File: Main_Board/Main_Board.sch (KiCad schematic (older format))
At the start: 68 parts, among them IC1 AZ1085CD-3.3TRG1, J1 PJ-037A, U1 STM32L152ZCTx, U2 LM386, Y1 ABM10W-16.0000MHZ-4-B1U-T3

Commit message: Reset_Line
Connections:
- net GND: no longer GPIOHeader1.1 (Pin_1)
- net Reset_Line: now reaches U1.87 (PG2)
- net Reset_Line: now also GPIOHeader1.1 (Pin_1)
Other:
- note added: "Speaker Circuit"
- note removed: "Hall Out Values"
- moved on the sheet: 5VOut1, BL1, BR1, C11, C24, C25, GPIOHeader1, J1, R8, TL1, TR1, Y1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

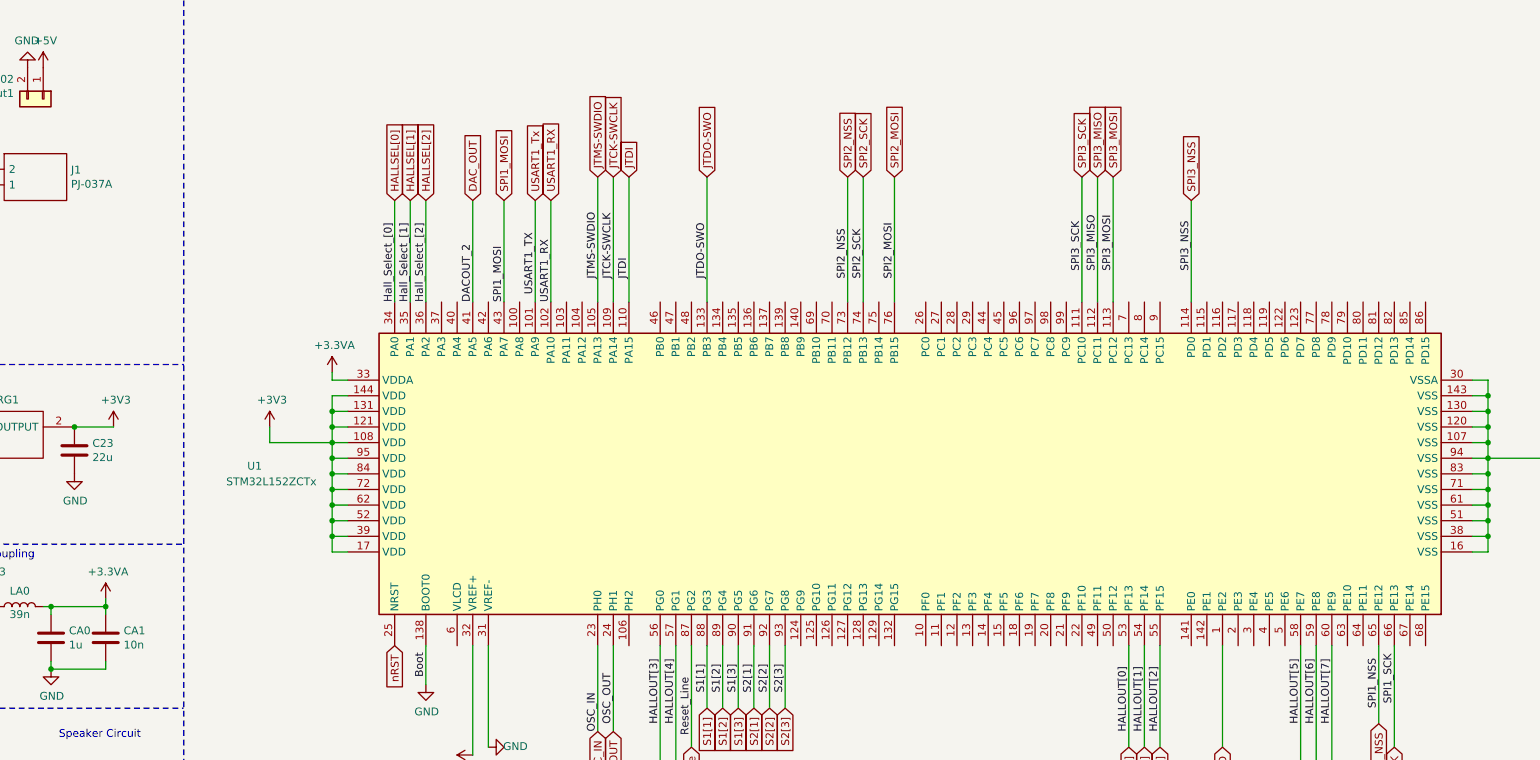
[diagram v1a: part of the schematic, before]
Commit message: final Rev1 changes. increased heatsink area, flipped LEDs again, increased button mount hole size
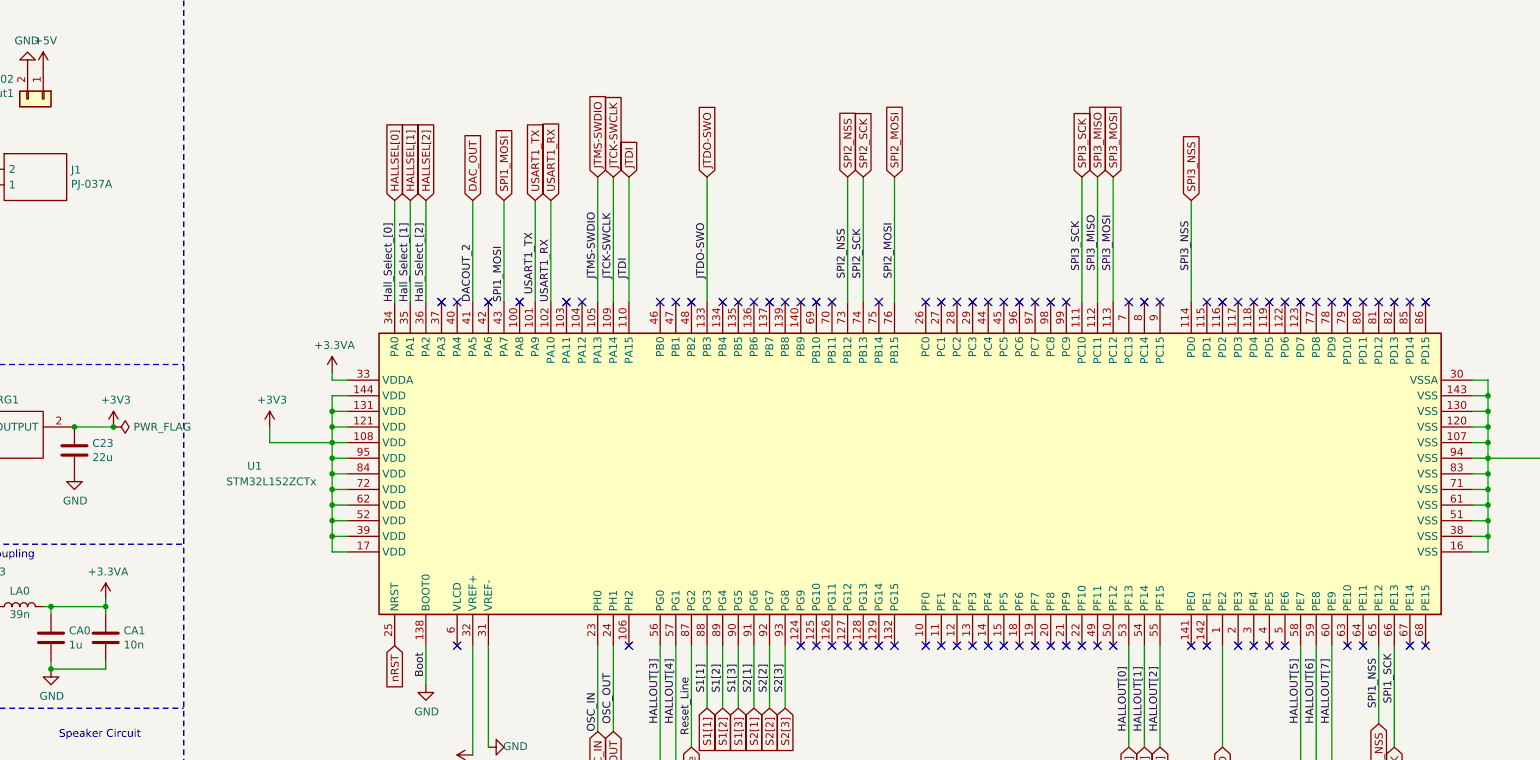
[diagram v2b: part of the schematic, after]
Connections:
- no-connect marks 3 -> 81
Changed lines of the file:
@@
 Analog Decoupling
 Text GLabel 15800 3900 1    50   Input ~ 0
-USART1_Tx
+USART1_TX
 Text GLabel 15900 3900 1    50   Input ~ 0
 USART1_RX
@@
 	1    0    0    -1
 $EndComp
-Wire Wire Line
-	12850 5350 13100 5350
 Connection ~ 12850 5350
 $Comp
@@
 Text GLabel 1400 8800 3    50   Input ~ 0
 Reset_Line
+$Comp
+L power:PWR_FLAG #FLG0101
+U 1 1 616BB65E
+P 13100 5350
+F 0 "#FLG0101" H 13100 5425 50  0001 C CNN
+F 1 "PWR_FLAG" V 13100 5478 50  0000 L CNN
+F 2 "" H 13100 5350 50  0001 C CNN
+F 3 "~" H 13100 5350 50  0001 C CNN
+	1    13100 5350
+	0    1    1    0
+$EndComp
+Connection ~ 13100 5350
+Wire Wire Line
+	12850 5350 13100 5350
+NoConn ~ 15200 4550
+NoConn ~ 15300 4550
+NoConn ~ 15500 4550
+NoConn ~ 15700 4550
+NoConn ~ 16000 4550
+NoConn ~ 16100 4550
+NoConn ~ 16600 4550
+NoConn ~ 16700 4550
+NoConn ~ 16800 4550
+NoConn ~ 17000 4550
+NoConn ~ 17100 4550
+NoConn ~ 17200 4550
+NoConn ~ 17300 4550
+NoConn ~ 17400 4550
+NoConn ~ 17500 4550
+NoConn ~ 17600 4550
+NoConn ~ 17700 4550
+NoConn ~ 18000 4550
+NoConn ~ 18300 4550
+NoConn ~ 18400 4550
+NoConn ~ 18500 4550
+NoConn ~ 18600 4550
+NoConn ~ 18700 4550
+NoConn ~ 18800 4550
+NoConn ~ 18900 4550
+NoConn ~ 19000 4550
+NoConn ~ 19100 4550
+NoConn ~ 19200 4550
+NoConn ~ 19600 4550
+NoConn ~ 19700 4550
+NoConn ~ 19800 4550
+NoConn ~ 20100 4550
+NoConn ~ 20200 4550
+NoConn ~ 20300 4550
+NoConn ~ 20400 4550
+NoConn ~ 20500 4550
+NoConn ~ 20600 4550
+NoConn ~ 20700 4550
+NoConn ~ 20800 4550
+NoConn ~ 20900 4550
+NoConn ~ 21000 4550
+NoConn ~ 21100 4550
+NoConn ~ 21200 4550
+NoConn ~ 21300 4550
+NoConn ~ 21400 4550
+NoConn ~ 21500 4550
+NoConn ~ 21500 6750
+NoConn ~ 21400 6750
+NoConn ~ 21100 6750
+NoConn ~ 21000 6750
+NoConn ~ 20600 6750
+NoConn ~ 20500 6750
+NoConn ~ 20400 6750
+NoConn ~ 20300 6750
+NoConn ~ 20000 6750
+NoConn ~ 20100 6750
+NoConn ~ 19500 6750
+NoConn ~ 19400 6750
+NoConn ~ 19300 6750
+NoConn ~ 19200 6750
+NoConn ~ 19100 6750
+NoConn ~ 19000 6750
+NoConn ~ 18900 6750
+NoConn ~ 18800 6750
+NoConn ~ 18700 6750
+NoConn ~ 18600 6750
+NoConn ~ 18500 6750
+NoConn ~ 18400 6750
+NoConn ~ 18300 6750
+NoConn ~ 18100 6750
+NoConn ~ 18000 6750
+NoConn ~ 17900 6750
+NoConn ~ 17800 6750
+NoConn ~ 17700 6750
+NoConn ~ 17600 6750
+NoConn ~ 17500 6750
+NoConn ~ 16400 6750
+NoConn ~ 15300 6750
 $EndSCHEMATC

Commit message: Some updates
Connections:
- removed net NC: U2.1 (GAIN), U2.7 (BYPASS), U2.8 (GAIN)
- no-connect marks 81 -> 84
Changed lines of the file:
@@
 	0    1    1    0
-$EndComp
-$Comp
-L Amplifier_Audio:LM386 U2
-U 1 1 6164CCD8
-P 10950 8700
-F 0 "U2" H 11294 8746 50  0000 L CNN
-F 1 "LM386" H 11294 8655 50  0000 L CNN
-F 2 "SamacSys_Parts:SOIC127P600X175-8N" H 11050 8800 50  0001 C CNN
-F 3 "http://www.ti.com/lit/ds/symlink/lm386.pdf" H 11150 8900 50  0001 C CNN
-	1    10950 8700
-	1    0    0    -1
 $EndComp
 Wire Wire Line
@@
 $EndComp
 Wire Wire Line
-	10950 8400 11050 8400
-Text GLabel 11050 8400 2    50   Input ~ 0
-NC
-Wire Wire Line
-	10950 9000 11050 9000
-Wire Wire Line
-	11150 9000 11150 8950
-Wire Wire Line
-	11150 8950 11200 8950
-Connection ~ 11050 9000
-Wire Wire Line
-	11050 9000 11150 9000
-Text GLabel 11200 8950 2    50   Input ~ 0
-NC
-Wire Wire Line
 	10650 9000 10850 9000
 Connection ~ 10650 9000
-Connection ~ 10850 9000
 $Comp
 L power:GND #PWR0113
@@
 	12050 9100 12050 9750
 Wire Wire Line
-	10850 9750 10850 9550
-Wire Wire Line
-	10850 9550 11100 9550
-Wire Wire Line
-	11100 9550 11100 9300
-Wire Wire Line
 	11100 9300 10850 9300
-Wire Wire Line
-	10850 9750 11650 9750
 Connection ~ 11650 9750
 Wire Wire Line
@@
 NoConn ~ 16400 6750
 NoConn ~ 15300 6750
+Connection ~ 10850 9000
+$Comp
+L Amplifier_Audio:LM386 U2
+U 1 1 6164CCD8
+P 10950 8700
+F 0 "U2" H 11294 8746 50  0000 L CNN
+F 1 "LM386" H 11294 8655 50  0000 L CNN
+F 2 "SamacSys_Parts:SOIC127P600X175-8N" H 11050 8800 50  0001 C CNN
+F 3 "http://www.ti.com/lit/ds/symlink/lm386.pdf" H 11150 8900 50  0001 C CNN
+	1    10950 8700
+	1    0    0    -1
+$EndComp
+NoConn ~ 10950 8400
+NoConn ~ 10950 9000
+NoConn ~ 11050 9000
+Wire Wire Line
+	11100 9750 11650 9750
+Wire Wire Line
+	11100 9300 11100 9750
 $EndSCHEMATC
